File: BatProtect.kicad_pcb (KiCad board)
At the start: 2 copper layers, 26.7 x 15.6 mm, 23 parts, among them J1 Bat, J2 Load, Q1 Q_PMOS_GDS, Q2 SI2308, SW1 SW_DIP_x01, U1 ATTINY13A, U2 MIC5219-5.0

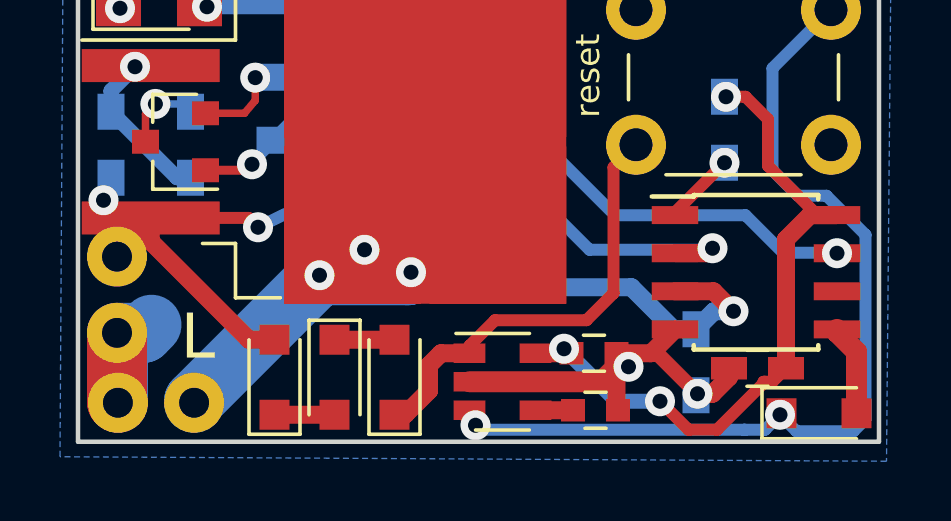
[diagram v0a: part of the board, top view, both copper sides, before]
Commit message: Adjust a bit schematic. Correct resistor divider
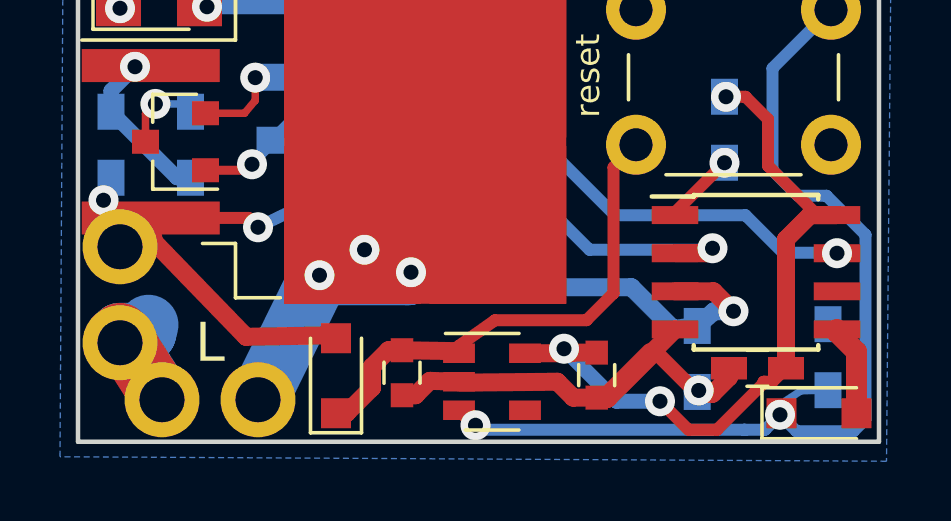
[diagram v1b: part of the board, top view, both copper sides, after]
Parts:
- removed D4, D5: D, Diodes_SMD:D_SOD-323_HandSoldering
- added R9: 10K, Resistors_SMD:R_0603_HandSoldering, B.Cu at (197.4, 119.7)
- C1: value 470p -> 10uf
- R3: value 10K -> 12K
- R4: value 3K -> 3.3K
- U1: value ATTINY13A -> ATTINY13A-SU
- U2: value MIC5219-5.0 -> MIC5235-5.0
- moved C1 6.57 mm to (183.2, 120.2), turned to 270 degrees
- moved D2 2.05 mm to (181.0, 120.3)
- moved J2 1.80 mm to (176.8, 121.1)
- moved C3 0.74 mm to (189.7, 120.3), turned to 270 degrees
- moved U2 0.35 mm to (186.2, 120.5)
- moved R4 0.12 mm to (193.0, 119.7)
- moved J1 0.10 mm to (173.8, 117.6)
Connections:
- D2 pad 1: Net-(D2-Pad1) -> Net-(C1-Pad1)
- SW1 pad 2: Net-(D5-Pad1) -> Net-(C1-Pad1)
- U2 pad 1: Net-(D5-Pad1) -> Net-(C1-Pad1)
- U2 pad 4: Net-(C1-Pad1) -> Net-(U2-Pad4)
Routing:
- net Net-(C1-Pad1): track 1.25 -> 16.7 mm
- net Net-(D5-Pad1): track 14.9 -> 0.00 mm
- net Net-(D3-Pad1): track 30.7 -> 33.0 mm
- net Net-(D4-Pad1): track 2.00 -> 0.00 mm
- net Net-(D2-Pad1): track 2.00 -> 0.00 mm
- net +BATT: track 19.7 -> 21.5 mm
- net Net-(C2-Pad1): track 23.5 -> 25.0 mm
- net Net-(J2-Pad1): track 27.3 -> 26.1 mm
- net GND: track 22.5 -> 23.6 mm, vias 4 -> 3
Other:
- board text added: "23V MAX!"
- board text removed: "21V MAX!"

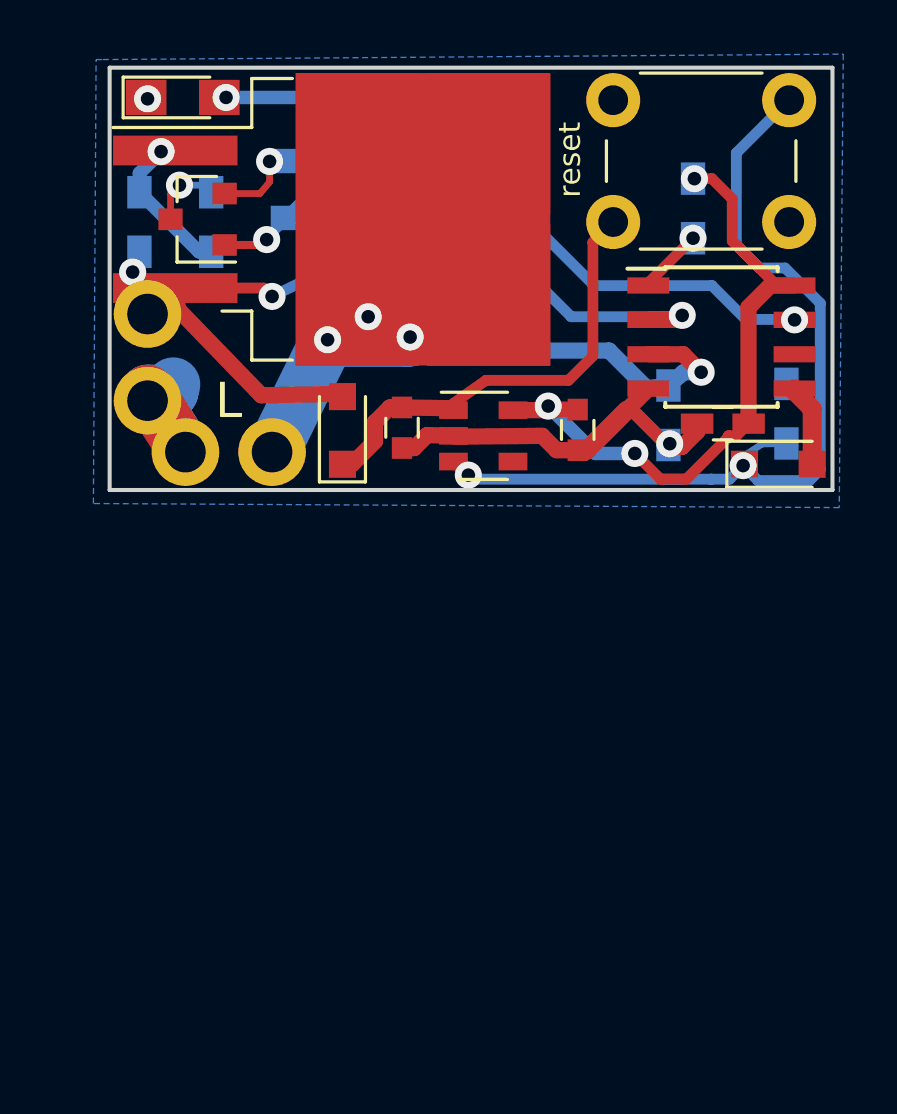
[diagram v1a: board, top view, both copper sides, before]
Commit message: Changed the mosfet to better one. PCB redesign
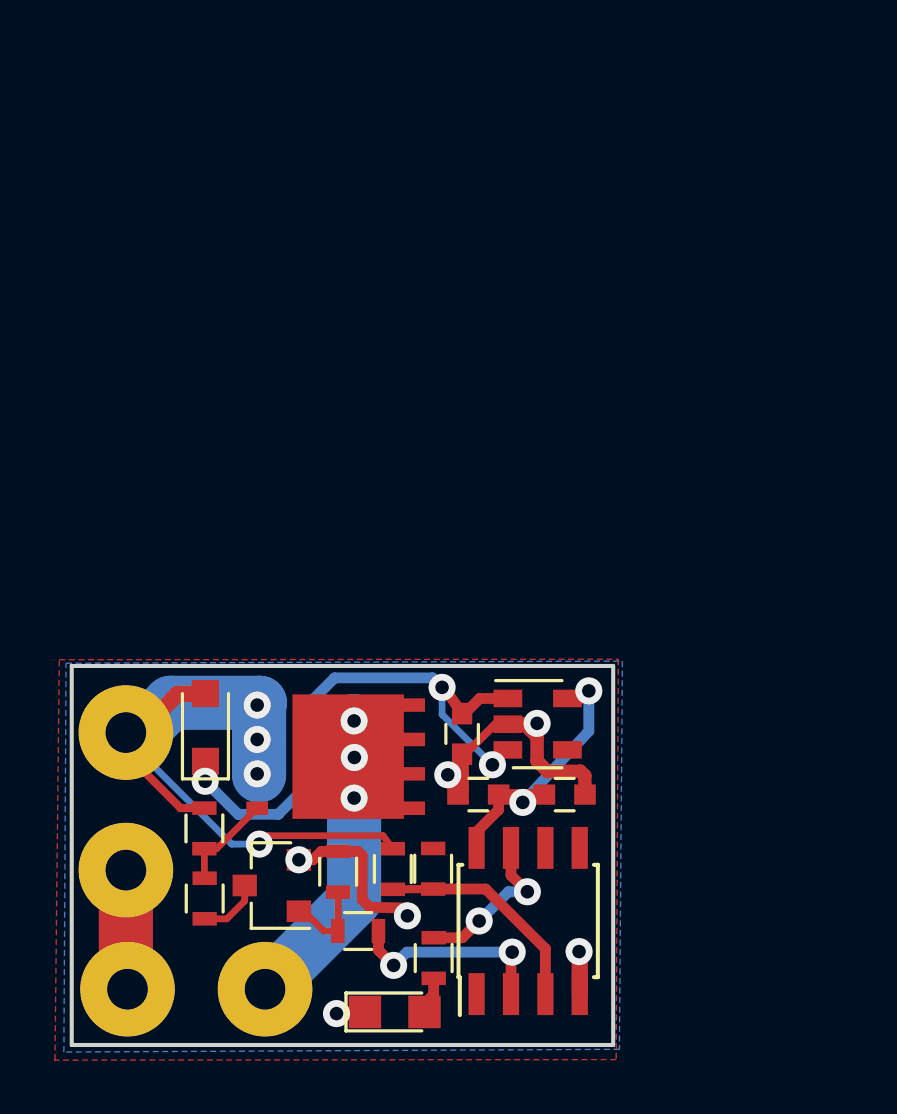
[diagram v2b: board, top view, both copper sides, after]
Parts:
- removed D3: D, Diodes_SMD:D_SOD-323_HandSoldering
- removed R7, R9: 10K, Resistors_SMD:R_0603_HandSoldering
- removed SW1: SW_DIP_x01, Buttons_Switches_THT:SW_PUSH_6mm
- C2: footprint Capacitors_SMD:C_0603_HandSoldering -> Capacitors_SMD:C_0603
- D1: footprint LEDs:LED_0805_HandSoldering -> LEDs:LED_0805
- J1, J2: footprint KiCad_custom:Conn2pin_2.54mm -> KiCadCustomLibs:Connector_2x5mm_1.5Drill
- Q1: value Q_PMOS_GDS -> AON6403; footprint TO_SOT_Packages_SMD:TO-263-2 -> KiCadCustomLibs:DFN-8-1EP_6x5mm
- R1, R2, R3, R4, R5, R6, R8: footprint Resistors_SMD:R_0603_HandSoldering -> Resistors_SMD:R_0603; moved to F.Cu
- moved D1 34.7 mm to (182.9, 141.8)
- moved R6 29.5 mm to (184.4, 139.8), turned to 90 degrees
- moved R5 26.4 mm to (181.6, 138.8)
- moved R2 26.3 mm to (180.8, 136.6), turned to 90 degrees
- moved R8 25.0 mm to (175.9, 137.6), turned to 270 degrees
- moved Q2 24.8 mm to (178.4, 137.1)
- moved U1 22.7 mm to (187.9, 138.4), turned to 90 degrees
- moved R3 22.6 mm to (182.9, 136.5), turned to 270 degrees
- moved R1 22.5 mm to (175.9, 135.0), turned to 270 degrees
- moved J2 19.9 mm to (175.6, 140.9)
- moved Q1 19.9 mm to (180.8, 132.3)
- moved R4 18.9 mm to (184.3, 136.5), turned to 90 degrees
- moved J1 16.4 mm to (173.0, 134.0)
- moved C2 14.9 mm to (189.2, 133.8), turned to 0 degrees
- moved C3 14.0 mm to (186.0, 133.8), turned to 180 degrees
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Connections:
- U1 pad 1: Net-(R7-Pad2) -> (no net)
- U1 pad 5: Net-(D3-Pad2) -> (no net)
- U1 pad 6: Net-(U1-Pad6) -> (no net)
- U2 pad 3: Net-(D3-Pad1) -> Net-(C1-Pad1)
- U2 pad 4: Net-(U2-Pad4) -> (no net)
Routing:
- net Net-(D3-Pad1): track 33.0 -> 0.00 mm, vias 2 -> 0
- net Net-(C2-Pad1): track 25.0 -> 11.3 mm, vias 3 -> 2
- net Net-(D1-Pad2): track 10.6 -> 1.38 mm, vias 1 -> 0
- net Net-(R6-Pad2): track 13.7 -> 6.03 mm, vias 1 -> 2
- net Net-(R5-Pad1): track 15.3 -> 7.65 mm, vias 1 -> 2
- net +BATT: track 21.5 -> 28.5 mm, vias 2 -> 4
- net Net-(R3-Pad2): track 13.9 -> 8.22 mm, vias 1 -> 0
- net Net-(C1-Pad1): track 16.7 -> 21.5 mm, vias 0 -> 3
- net Net-(J2-Pad1): track 26.1 -> 29.3 mm, vias 3 -> 4
- net Net-(D3-Pad2): track 3.06 -> 0.00 mm
- net Net-(Q2-Pad1): track 5.81 -> 3.19 mm, vias 1 -> 0
- net Net-(R7-Pad2): track 2.43 -> 0.00 mm, vias 1 -> 0
- net Net-(Q1-Pad1): track 5.98 -> 3.66 mm, vias 1 -> 0
- net Net-(Q2-Pad3): track 3.14 -> 2.32 mm, vias 1 -> 0
- net GND: track 23.6 -> 24.1 mm, vias 3 -> 6
- added copper zone on F.Cu, net GND
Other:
- board size 26.7 x 15.6 mm -> 20 x 14 mm
- board text added: "+"
- board text added: "-"
- board text removed: "L"
- board text removed: "reset"
